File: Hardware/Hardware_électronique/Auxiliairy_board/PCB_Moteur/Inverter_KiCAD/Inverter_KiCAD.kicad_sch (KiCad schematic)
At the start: 17 parts, among them J1 Conn_02x02_Top_Bottom, J101 Conn_01x02, J2 Conn_02x03_Top_Bottom

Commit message: Add files via upload
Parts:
- removed J2: Conn_02x03_Top_Bottom, Connector_Molex:Molex_Mega-Fit_76825-0006_2x03_P5.70mm_Horizontal, symbol Connector_Generic:Conn_02x03_Top_Bottom
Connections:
- net V_output is gone; now on net GND: J1.2 (Pin_2)
- net W_output: no longer names the net of J1.3 (Pin_3)
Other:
- removed sheet Arm_IRF540NBbF1
- removed sheet Arm_IRF540NBbF2
- removed sheet V_Power_LED
- removed sheet break
- removed sheet pwrSupply_5V
- sheet pwrSupplyFiltering ports: added ISO_15V, ISO_GND, PwrEn, VSupply_AB, VSupply_BB, Vbus; removed none
- note added: "pwr Supply"
- note removed: "Break for reverse current protection"

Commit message: update schematic
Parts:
- removed H101, H102, H103, H104, H105, H106, H107, H108: MountingHole_Pad, MountingHole:MountingHole_3.2mm_M3_Pad_Via, symbol Mechanical:MountingHole_Pad
- removed J101: Conn_01x02, Custom:691311500102, symbol Connector_Generic:Conn_01x02
- added BT1: Battery, symbol Device:Battery
- added C1, C4: 10u, Capacitor_SMD:C_2220_5650Metric, symbol Device:C_Small
- added C10, C11, C12, C8, C9: 1.5m, Capacitor_THT:CP_Radial_D35.0mm_P10.00mm_SnapIn, symbol Device:C_Polarized
- added C13, C14, C15, C5, C6, C7: 4.7n, Capacitor_SMD:C_0402_1005Metric, symbol Device:C_Small
- added C16: 10n, Capacitor_SMD:C_0402_1005Metric, symbol Device:C_Small
- added C17: 10u, Capacitor_SMD:CP_Elec_4x5.4, symbol Device:C_Polarized
- added C18: 22u, Capacitor_SMD:CP_Elec_5x5.4, symbol Device:C_Polarized
- added C19: 100n, Capacitor_SMD:C_0402_1005Metric, symbol Device:C_Small
- added C2, C3: 1u, symbol Device:C_Small
- added D1, D2, D3, D4, D5, D6, D7, D8: Red LED, LED_SMD:LED_0603_1608Metric, symbol Device:LED
- added J2: 173010542, Buck_5V_173010542:173010542, symbol 173010542_5V_Buck:173010542
- added J3: Conn_02x05_Odd_Even, symbol Connector_Generic:Conn_02x05_Odd_Even
- added J4, J5: Conn_01x02, Connector_JST:JST_XH_B2B-XH-A_1x02_P2.50mm_Vertical, symbol Connector_Generic:Conn_01x02
- added Q1, Q2, Q3, Q4: IRF540N, Package_TO_SOT_THT:TO-220-3_Vertical, symbol Transistor_FET:IRF540N
- added Q5: SQ2310ES, Package_TO_SOT_SMD:SOT-23, symbol Device:Q_NMOS_GSD
- added R1, R10, R4, R7, R8: 390, Resistor_SMD:R_0402_1005Metric, symbol Device:R_Small
- added R11: 22, Resistor_SMD:R_0402_1005Metric, symbol Device:R_Small
- added R12: 10k, Resistor_SMD:R_0402_1005Metric, symbol Device:R_Small_US
- added R2: 10k, Resistor_SMD:R_0402_1005Metric, symbol Device:R_Small
- added R3: 470k, Resistor_SMD:R_0402_1005Metric, symbol Device:R_Small
- added R5: 1k, Resistor_SMD:R_0402_1005Metric, symbol Device:R_Small
- added R6: 2k7, Resistor_SMD:R_0402_1005Metric, symbol Device:R_Small
- added R9: 680, Resistor_SMD:R_0402_1005Metric, symbol Device:R_Small
- added U1: MIC4606, symbol mic4606:MIC4606
- added U2: GO 10-SME/SP3, Custom:SOIC8-GO-SME&slash_SP3_LEM, symbol Custom:GO_10-SME
- added U3: GO 10-SME/SP3, SOIC8-GO-SME/SP3_LEM, symbol Custom:GO_10-SME
- added U4: AZ1117-3.3, Package_TO_SOT_SMD:SOT-223-3_TabPin2, symbol Regulator_Linear:AZ1117-3.3
- added U5: MAX3097ECSE+, Package_SO:SOIC-16_3.9x9.9mm_P1.27mm, symbol Custom:MAX3097ECSE+
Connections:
- net ENC_A: now also U5.14 (OutA)
- net ENC_B: now also U5.12 (OutB)
- net GND: now also BT1.2 (-), C1.2, C10.2, C11.2, C12.2, C13.2, C14.2, C15.2, C16.2, C17.2, C18.2, C19.2, C4.2, C5.2, C6.2, C7.2, C8.2, C9.2, J2.2 (GND), J3.3 (Pin_3), Q2.3 (S), Q4.2 (D), Q5.2 (S), R1.2, R10.2, R12.2, R2.2, R4.2, R5.2, R6.2, R7.2, R8.2, R9.2, U2.5 (GND), U3.5 (GND), U4.1 (GND), U5.7 (GND)
- net ISO_15V: now also U1.12 (VDD)
- net ISO_GND: now also U1.13 (VSS)
- net Vbus: now also C1.1, C4.1, Q1.2 (D), Q3.3 (S)
- net ARM_B: now reaches J1.3 (Pin_3)
- net ARM_B: now also C2.2, Q3.2 (D), Q4.3 (S), U1.15 (BHS)
- net U_output renamed ARM_OUT_A
- net ARM_OUT_A: now also U3.3 (IP-), U3.4 (IP-)
- new net: D8.1 (K), R10.1
- new net: D1.1 (K), R1.1
- new net: J4.2 (Pin_2), J5.2 (Pin_2), Q5.3 (D)
- new net: Q5.1 (G), R11.1, R12.1
- new net: C3.2, U1.8 (AHB)
- new net: C2.1, U1.1 (BHB)
- new net: D3.1 (K), R6.1
- new net: D4.1 (K), R4.1
- new net: D2.1 (K), R2.1
- new net: D7.1 (K), R8.1
- new net: D5.1 (K), R7.1
- new net: BT1.1 (+), U2.1 (IP+), U2.2 (IP+)
- new net: D6.1 (K), R9.1
- new net +3.3V: C13.1, C18.1, C19.1, D8.2 (A), J3.2 (Pin_2), U2.8 (UC), U4.2 (VO), U5.16 (VCC)
- new net +5V: C17.1, D6.2 (A), J2.3 (VOUT), J4.1 (Pin_1), J5.1 (Pin_1), U4.3 (VI)
- new net A: J3.6 (Pin_6), U5.1 (A)
- new net ARM_IN_A: C3.1, Q1.3 (S), Q2.2 (D), U1.10 (AHS), U3.1 (IP+), U3.2 (IP+)
- new net B: J3.8 (Pin_8), U5.3 (B)
- new net Cmd_H_A: Q1.1 (G), U1.16 (BHO), U1.9 (AHO)
- new net Cmd_H_B: Q3.1 (G)
- new net Cmd_L_A: Q2.1 (G), U1.11 (ALO)
- new net Cmd_L_B: Q4.1 (G), U1.14 (BLO)
- new net ENC_C: U5.10 (OutZ)
- new net ISO_3.3V: C5.1, U3.8 (UC)
- new net I_mes: C6.1, U3.7 (UOUT)
- new net Imes: C14.1, U2.7 (UOUT)
- new net In_A_H: D1.2 (A), U1.6 (AHI)
- new net In_A_L: D4.2 (A), U1.5 (ALI)
- new net In_B_H: D5.2 (A), U1.3 (BHI)
- new net In_B_L: D7.2 (A), U1.4 (BLI)
- new net PWM_FAN: R11.2
- new net PwrEn: U1.2 (EN)
- new net Uref: C15.1, C7.1, U2.6 (UREF), U3.6 (UREF)
- new net VBUS: C10.1, C11.1, C12.1, C8.1, C9.1, D2.2 (A), D3.2 (A), J2.1 (VIN), R3.1, U2.3 (IP-), U2.4 (IP-)
- new net VBus_Sense: C16.1, R3.2, R5.1
- new net Z: J3.10 (Pin_10), U5.5 (Z)
- new net /A: J3.5 (Pin_5), U5.2 (/A)
- new net /B: J3.7 (Pin_7), U5.4 (/B)
- new net /Z: J3.9 (Pin_9), U5.6 (/Z)
- no-connect marks 3 -> 8
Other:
- removed sheet Arm_IRF540NBbF
- removed sheet FAN
- removed sheet MCU_STM32G474
- removed sheet Vbus_Sense
- removed sheet encoderMotor
- removed sheet pwrSupply
- removed sheet pwrSupplyFiltering
- added sheet MCU_STM32G475 (MCU_STM32G474.kicad_sch)
- sheet tempSensor ports: added none; removed ISO_3V3, ISO_GND
- note added: "ADD UREF"
- note added: "Based on Wurth 173010542 Vin : 7V-42V Vout : 5V Max : 1A"
- note added: "Batt = Connector for battery"
- note added: "Check ratio Voltage Divider Vmax = 29.6V VBus_sense = 3.3V max"
- note added: "Driver"
- note added: "Hall current"
- note added: "Mosfet"
- note added: "Motor Driver"
- note added: "Vin+ max value : 0.41V"
- note added: "Wurth Capacitor : 861011086027 1.5mF / 200V"
- note removed: "Bus mesurement Current and voltage"
- note removed: "Chopper 3x Half-bridges"
- note removed: "Feedback motor enc"
- note removed: "Input Supply and DC/DC converters"
- note removed: "Power Side"
- note removed: "pwr Supply"
- moved on the sheet: H109, H110, H111, H112, H113, H114

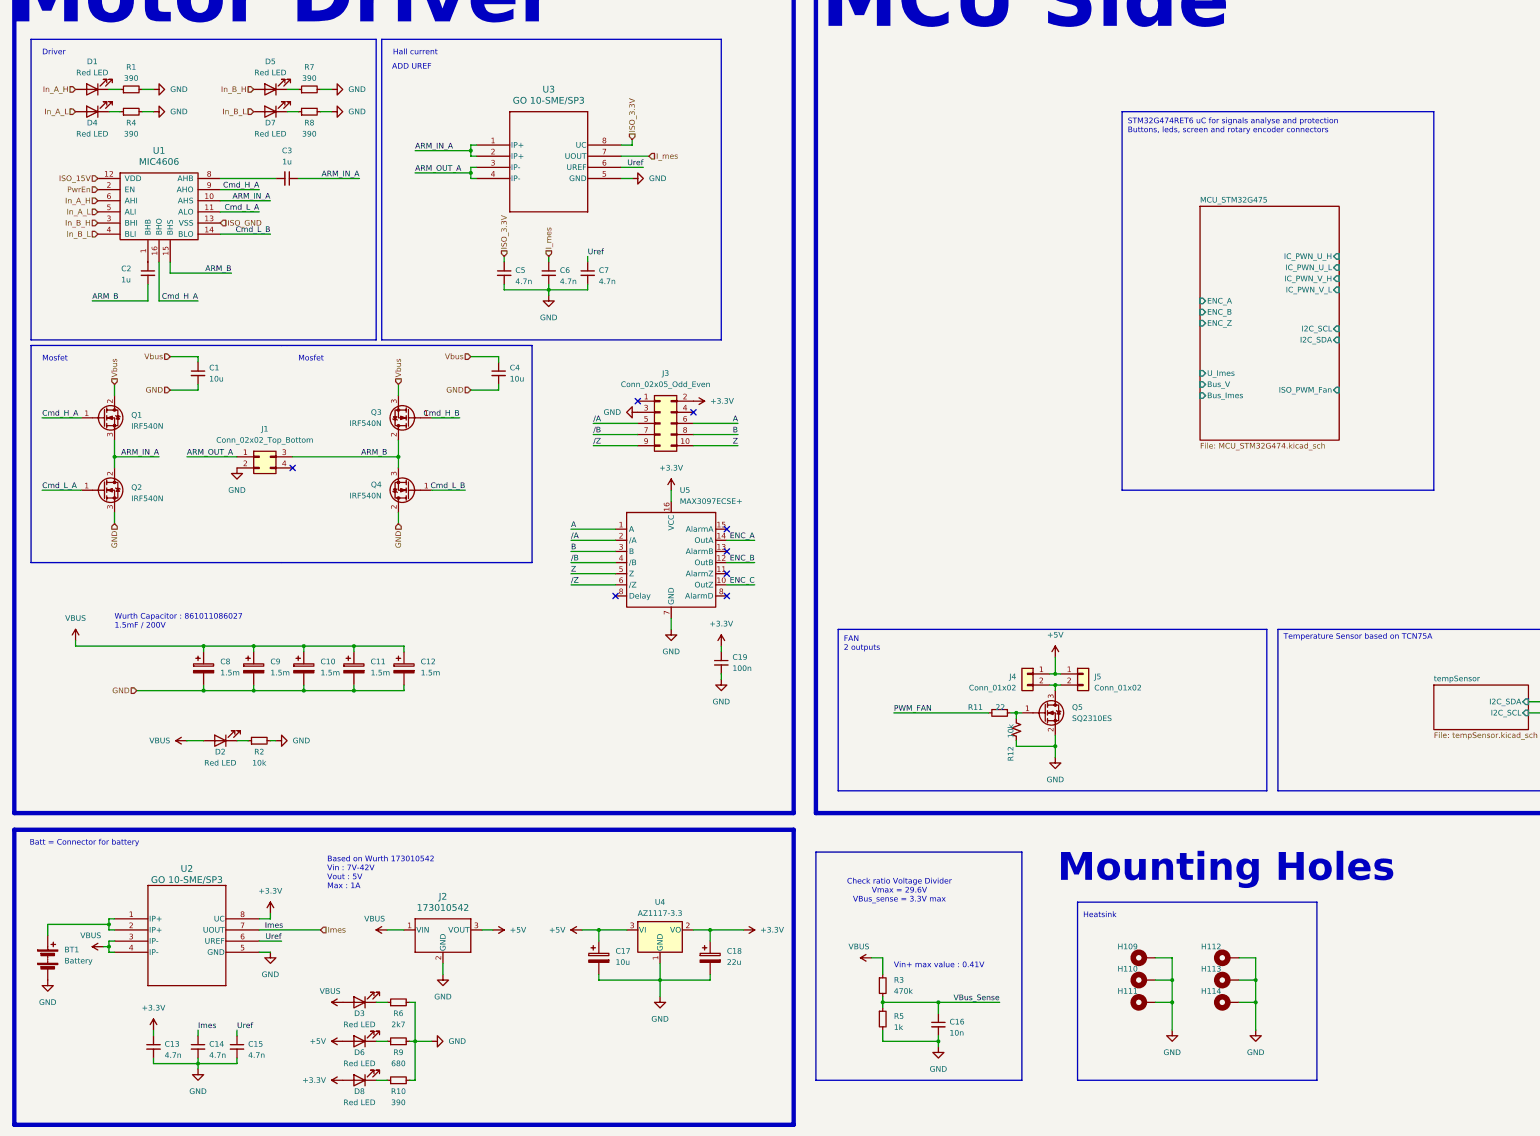
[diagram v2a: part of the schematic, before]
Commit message: update schematic
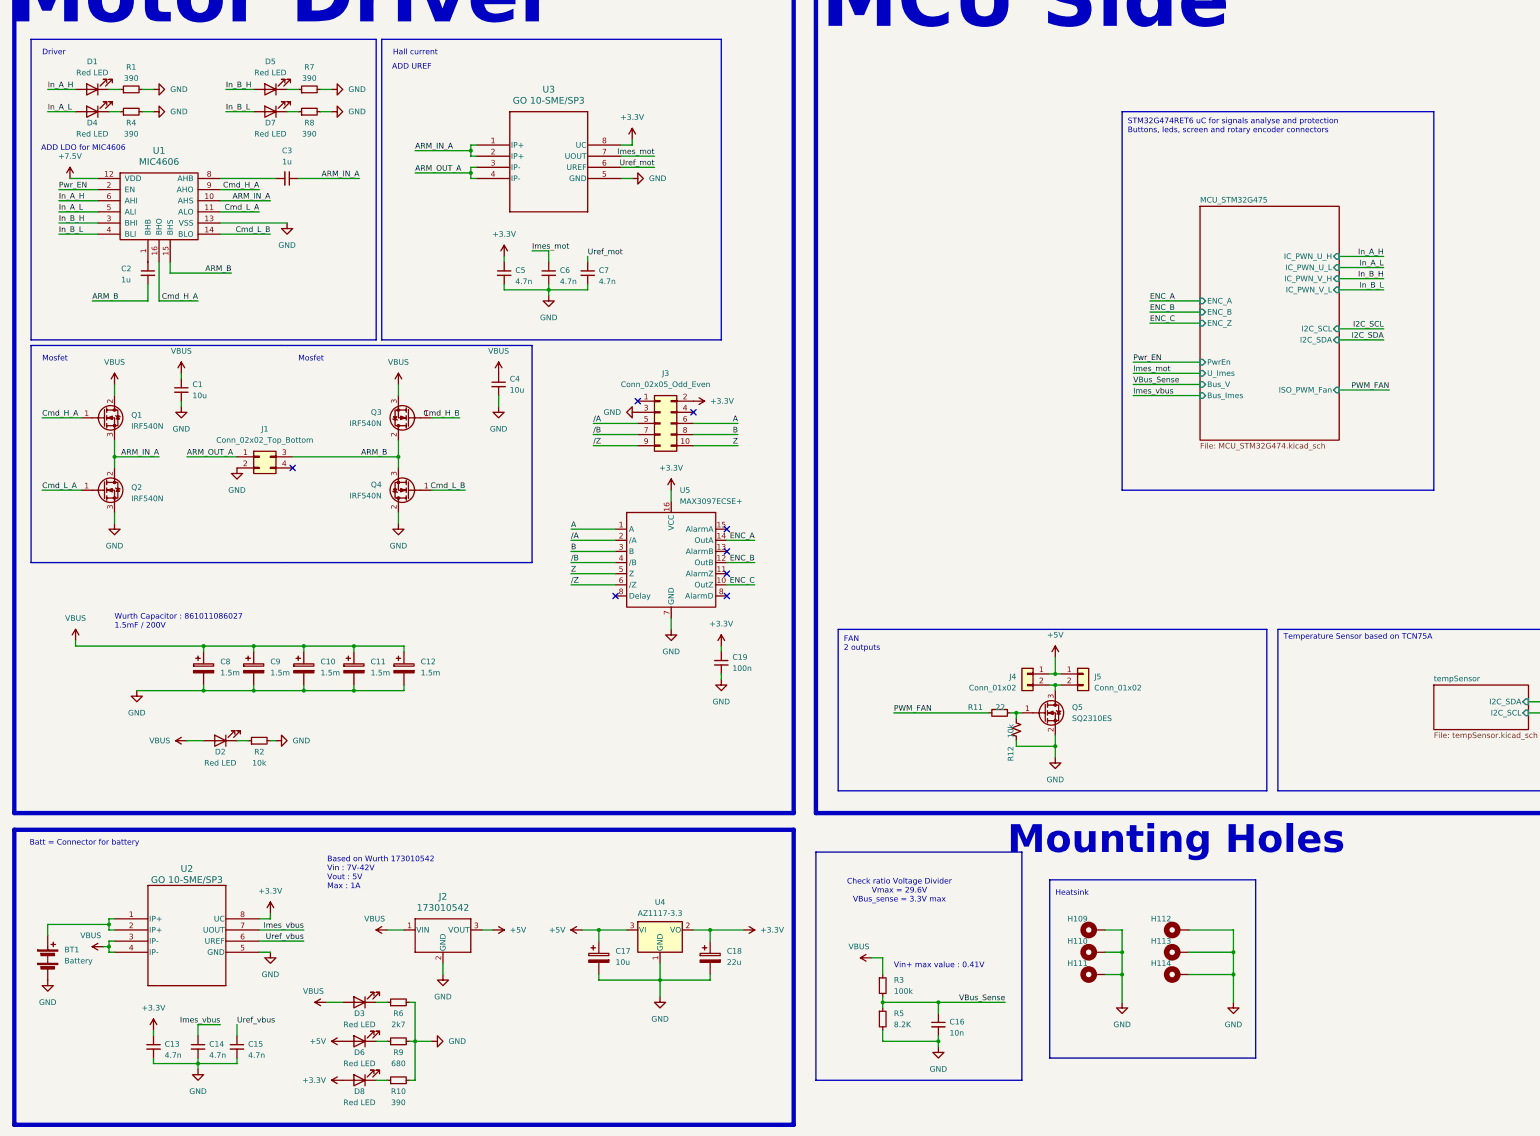
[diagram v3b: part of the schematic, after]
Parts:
- R3: value 470k -> 100k
- R5: value 1k -> 8.2K
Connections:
- net ISO_3.3V is gone; now on net +3.3V: C5.1, U3.8 (UC)
- net ISO_GND is gone; now on net GND: U1.13 (VSS)
- net Vbus is gone; now on net VBUS: C1.1, C4.1, Q1.2 (D), Q3.3 (S)
- net ISO_15V renamed +7.5V
- net I_mes renamed Imes_mot
- net Imes renamed Imes_vbus
- net PwrEn renamed Pwr_EN
- net Uref renamed Uref_mot
- net Uref_mot: no longer C15.1, U2.6 (UREF)
- new net Uref_vbus: C15.1, U2.6 (UREF)
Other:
- sheet MCU_STM32G475 ports: added PwrEn; removed none
- note added: "ADD LDO for MIC4606"
- moved on the sheet: C1, C4, H109, H110, H111, H112, H113, H114

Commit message: Add files via upload
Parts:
- added C33: 10u, symbol Device:C
- added C34: 4.7nF, symbol Device:C
- added C35: 22nF, symbol Device:C
- added C36: 47u, symbol Device:C
- added Converter_DCDC_WPMDH1: ~, Custom:Converter_DCDC, symbol Custom:Converter_DCDC
- added F1: Fuse, Custom:0031.8201, symbol Device:Fuse
- added J7: Conn_01x02_Pin, Connector_AMASS:AMASS_XT60PW-F_1x02_P7.20mm_Horizontal, symbol Connector:Conn_01x02_Pin
- added R26: 287k, symbol Device:R
- added R27: 1.91k, symbol Device:R
- added R28: 34k, symbol Device:R
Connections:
- new net: C34.1, Converter_DCDC_WPMDH1.5 (SS)
- new net: F1.1, J7.2 (Pin_2)
- new net: C35.2, Converter_DCDC_WPMDH1.6 (FB), R27.1, R28.2
- new net: C33.1, Converter_DCDC_WPMDH1.1 (Vin), Converter_DCDC_WPMDH1.3 (EN), J7.1 (Pin_1), R26.1
- new net: Converter_DCDC_WPMDH1.2 (RON), R26.2
- new net ISO_15V: C35.1, C36.1, Converter_DCDC_WPMDH1.7 (Vout), R28.1
- new net ISO_GND: C33.2, C34.2, C36.2, Converter_DCDC_WPMDH1.4 (AGND), Converter_DCDC_WPMDH1.8 (PGND), F1.2, R27.2

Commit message: last schematic editing
just miss a  FB resistor value
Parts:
- removed F1: Fuse, Custom:0031.8201, symbol Device:Fuse
- removed J7: Conn_01x02_Pin, Connector_AMASS:AMASS_XT60PW-F_1x02_P7.20mm_Horizontal, symbol Connector:Conn_01x02_Pin
- removed Q1, Q2, Q3, Q4: IRF540N, Package_TO_SOT_THT:TO-220-3_Vertical, symbol Transistor_FET:IRF540N
- added TP1, TP2, TP3, TP4: TestPoint, symbol Connector:TestPoint
- added U7, U8: CSD86350Q5D, DQY0008A, symbol CSD87351Q5D:CSD86350Q5D
- renumbered Converter_DCDC_WPMDH1 to Converter_DCDC_WPMDH1302401
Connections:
- net ISO_15V is gone; now on net +7.5V: C35.1, C36.1, Converter_DCDC_WPMDH1302401.7 (Vout), R28.1
- net ISO_GND is gone; now on net GND: C33.2, C34.2, C36.2, Converter_DCDC_WPMDH1302401.4 (AGND), Converter_DCDC_WPMDH1302401.8 (PGND), R27.2
- net +3.3V: now also TP4.1
- net +5V: now also TP3.1
- net +7.5V: now also J2.1 (VIN), TP2.1
- net ARM_B: now also U8.6 (VSW), U8.7 (VSW), U8.8 (VSW)
- net ARM_IN_A: now also U7.6 (VSW), U7.7 (VSW), U7.8 (VSW)
- net Cmd_H_A: now also U7.3 (TG); no longer U1.16 (BHO)
- net Cmd_H_B: now also U1.16 (BHO), U8.3 (TG)
- net Cmd_L_A: now also U7.5 (BG)
- net Cmd_L_B: now also U8.5 (BG)
- net GND: now also U7.9 (PGND), U8.9 (PGND)
- net VBUS: now also C33.1, Converter_DCDC_WPMDH1302401.1 (Vin), Converter_DCDC_WPMDH1302401.3 (EN), R26.1, TP1.1, U7.1 (VIN), U7.2 (VIN), U8.1 (VIN), U8.2 (VIN); no longer J2.1 (VIN)
- no-connect marks 8 -> 10
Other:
- note added: "Mounting holes"
- note added: "Vmax = 29.6V VBus_sense = 3.3V max"
- note added: "check FB resistors"
- note removed: "Check ratio Voltage Divider Vmax = 29.6V VBus_sense = 3.3V max"
- note removed: "Heatsink"
- note removed: "Mounting Holes"
- note removed: "Vin+ max value : 0.41V"
- moved on the sheet: C16, C17, C18, C33, C34, C35, C36, C4, Converter_DCDC_WPMDH1302401, H109, H110, H111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

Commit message: deut routage
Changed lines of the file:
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@@
 	)
 	(rectangle
-		(start 15.24 210.82)
-		(end 193.04 13.97)
+		(start 15.24 13.97)
+		(end 193.04 210.82)
 		(stroke
 			(width 1)
